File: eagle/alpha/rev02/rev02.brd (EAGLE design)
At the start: 100 x 80 mm, 382 parts, among them CN1 HOST, CN2 HOST, IC1 N25Q128A13ES, IC2 74AC244DW, IC3 N25Q128A13ES, J1 STM32-SWD, Q1 2N7002, Q2 BC818, Q4 2N7002, Q5 ASFL1, Q6 2N7002, T1 BC847, T2 BC847, U1 LMZ13608, U10 ATTINY828R-AU, U11 MC14551BDG, U12 23K640-I/SN, U13 XC7A200TFBG484, U14 EN6347QI, U15 EN6347QI, U16 EN5364QI, U2 LT3060ITS8-15, U3 MC74HC1G14DTT1G, U4 STM32F429BIT6, U5 IS45S32160F, U6 IS45S32160F, U7 MCP79412-I/SN, U8 FT232H_SERIAL, U9 FT232H_SERIAL, Y1 12 MHz, Y2 12 MHz

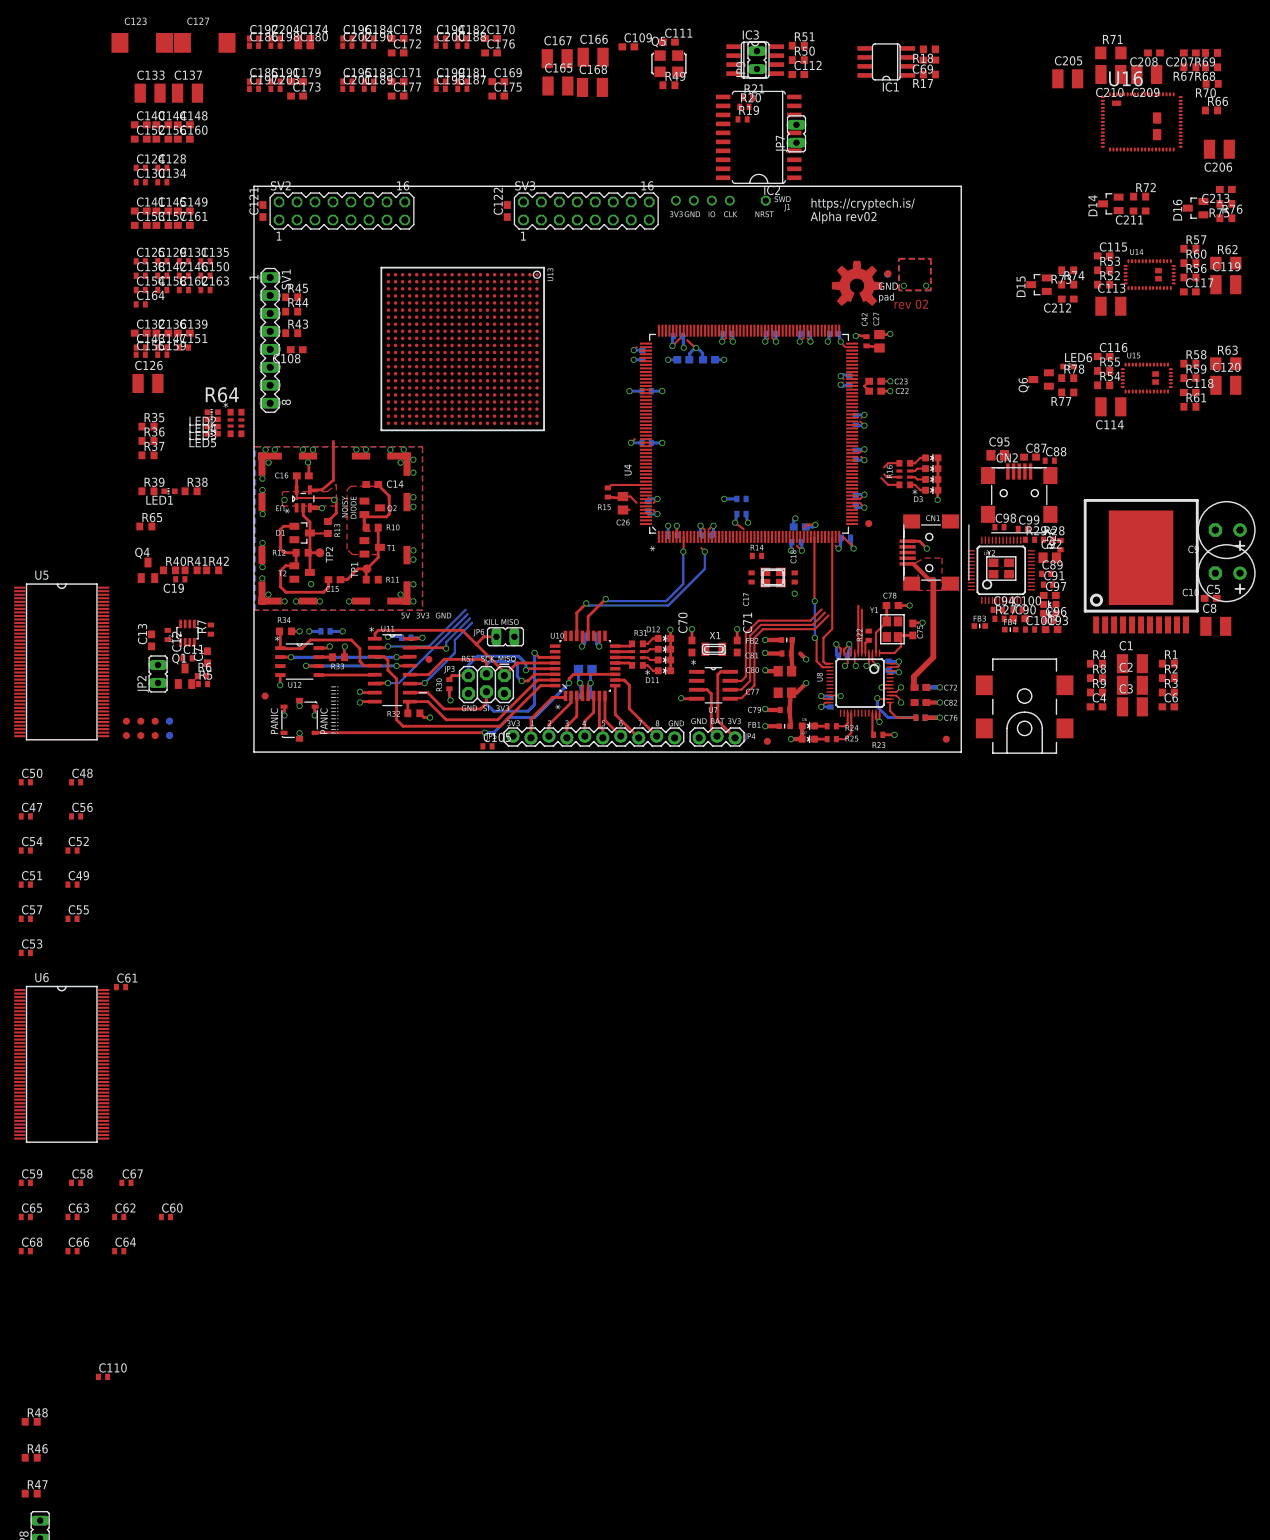
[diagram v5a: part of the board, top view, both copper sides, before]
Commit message: optimize BOM a bit, change more 0603s to 0402s
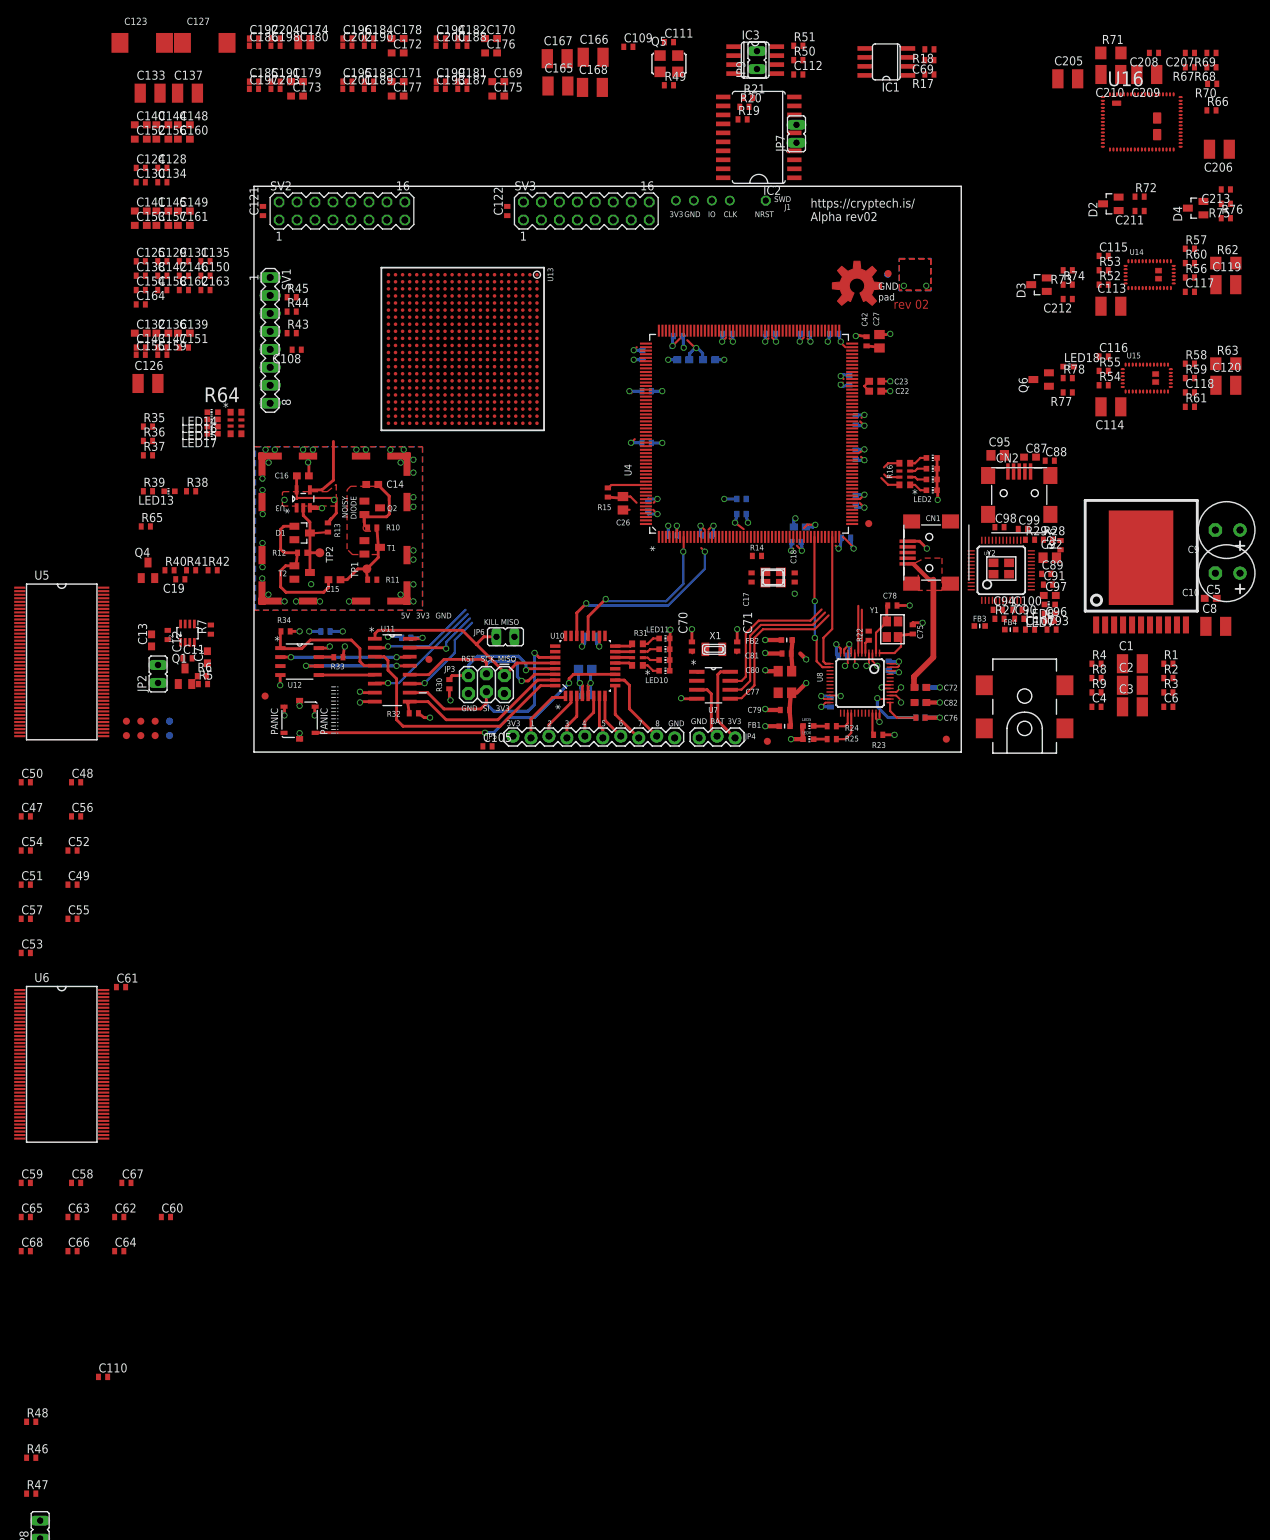
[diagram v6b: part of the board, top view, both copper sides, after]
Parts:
- removed D10, D7, D9: GREEN, SparkFun-LED:LED-0603
- removed D11: RED, SparkFun-LED:LED-0603
- removed D12: BLUE, SparkFun-LED:LED-0603
- removed D13, D5, D6, D8: YELLOW, SparkFun-LED:LED-0603
- removed D14, D15, D16: BAT54, diode:SOT23
- added LED10, LED13, LED14: RED, led:CHIP-LED0603
- added LED11, LED17: BLUE, led:CHIP-LED0603
- added LED12, LED16, LED7: YELLOW, led:CHIP-LED0603
- added LED15, LED18, LED8, LED9: GREEN, led:CHIP-LED0603
- C10, C9: value 330uF -> 330 uF
- C108, C109, C111, C112, C117, C118, C121, C122, C208, C211, C212, C213, C69: device resistor:C0603 -> resistor:C0402
- C11, C12: value 10NF -> 0.01 uF
- C110, C19, C20, C30, C32, C33, C34, C35, C36, C37, C38, C39, C40, C41, C42, C43, C44, C45, C46, C49, C51, C52, C53, C54, C55, C56, C57, C60, C62, C63, C64, C65, C66, C67, C68: value 0.1uF -> 0.1 uF
- C115, C116, C207, C4, C6: value 0.047uF -> 0.047 uF; device resistor:C0603 -> resistor:C0402
- C13, C7: value 2.2 uF LowESR -> 2.2 uF
- C14, C15, C16: device rcl:C0603 -> resistor:C0603
- C5: value 0.47uF -> 0.47 uF
- C70, C71: value 5pF -> 5 pF; device rcl:C0603 -> resistor:C0402
- C75, C78, C90, C93: device rcl:C0603 -> resistor:C0402
- D2: value GREEN -> BAT54; device SparkFun-LED:LED-0603 -> diode:SOT23
- D3: value RED -> BAT54; device SparkFun-LED:LED-0603 -> diode:SOT23
- D4: value BLUE -> BAT54; device SparkFun-LED:LED-0603 -> diode:SOT23
- LED1: value RED -> GREEN
- LED3: value GREEN -> BLUE
- LED5: value BLUE -> YELLOW
- R1, R10, R17, R18, R2, R3, R35, R36, R37, R38, R39, R4, R40, R41, R42, R43, R44, R45, R46, R47, R48, R49, R50, R51, R52, R53, R54, R55, R56, R57, R58, R59, R60, R61, R65, R66, R67, R68, R69, R70, R72, R73, R74, R75, R76, R77, R78, R8, R9: device resistor:R0603 -> resistor:R0402
- R11, R13: value 1K -> 1k; device resistor:R0603 -> resistor:R0402
- R12: value 10K -> 10k; device resistor:R0603 -> resistor:R0402
- R15, R19, R20, R21, R23, R27, R6, R7: value 10K -> 10k
- R22, R26: value 12K -> 12k
- R30: value 15K -> 15k
- R32, R33, R34: value 15K -> 15k; device resistor:R0603 -> resistor:R0402
- R5: value 1K -> 1k
- moved LED1 107.8 mm to (115.9, 40.8), turned to 270 degrees
- moved LED2 102.3 mm to (115.9, 37.7), turned to 270 degrees
- moved LED4 102.0 mm to (115.9, 39.3), turned to 270 degrees
- moved LED3 101.8 mm to (115.9, 42.3), turned to 270 degrees
- moved LED5 93.8 mm to (98.5, 4.41), turned to 270 degrees
- moved LED6 64.2 mm to (98.5, 2.54)
- moved D4 51.4 mm to (153.2, 77.6), turned to 90 degrees
- moved D2 45.2 mm to (141.2, 78.2), turned to 90 degrees
- moved D3 32.8 mm to (131.1, 66.8), turned to 90 degrees
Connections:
- net FPGA_DONE_INT: now also LED13.C; no longer LED1.C
- net FT_MGMT_VCC3V3: now also LED7.A, LED8.A; no longer D8.A, D9.A
- net FT_VCC3V3: now also LED5.A, LED6.A; no longer D6.A, D7.A
- net GND: now also LED1.C, LED10.C, LED11.C, LED12.C, LED14.C, LED15.C, LED16.C, LED17.C, LED9.C; no longer D10.C, D11.C, D12.C, D13.C, D2.C, D3.C, D4.C, D5.C, LED5.C
- net N$15: now also LED12.A; no longer D13.A
- net N$16: now also LED10.A; no longer D11.A
- net N$17: now also LED3.A; no longer D4.A
- net N$18: now also LED1.A; no longer D2.A
- net N$19: now also LED4.A; no longer D5.A
- net N$20: now also LED2.A; no longer D3.A
- net N$24: now also LED5.C; no longer D6.C
- net N$26: now also LED6.C; no longer D7.C
- net N$27: now also LED17.A; no longer LED5.A
- net N$28: now also LED15.A; no longer LED3.A
- net N$29: now also LED16.A; no longer LED4.A
- net N$30: now also LED14.A; no longer LED2.A
- net N$34: now also LED13.A; no longer LED1.A
- net N$4: now also LED11.A; no longer D12.A
- net N$5: now also LED9.A; no longer D10.A
- net N$50: now also LED18.C; no longer LED6.C
- net N$51: now also LED18.A; no longer LED6.A
- net N$6: now also LED7.C; no longer D8.C
- net N$7: now also LED8.C; no longer D9.C
- net POK_VCCAUX: now also D3.3; no longer D15.3
- net POK_VCCINT: now also D4.3; no longer D16.3
- net PWR_ENA_VCCAUX: now also D4.1; no longer D16.1
- net PWR_ENA_VCCINT: now also D2.1; no longer D14.1
- net PWR_ENA_VCCO: now also D3.1; no longer D15.1
- net VCC_5V0: now also D2.3; no longer D14.3
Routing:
- net GND: track 139.6 -> 140.6 mm
- net AMPLIFIED: track 14.0 -> 14.5 mm

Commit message: First set of updates based on review feedback.
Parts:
- removed R17: 4.7k, resistor:R0402
- C13, C7: value 2.2 uF -> 4.7 uF
- R24, R25, R28, R29: value 220 -> 330
- moved R4 198.2 mm to (-11.4, -115.6)
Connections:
- removed net N$53: R4.2, U1.P$3
- new net N$3: Q5.3, R4.2
- net FPGA_GCLK: no longer Q5.3
- net GND: now also C22.1, C23.1, C24.1, C25.1, U1.3, U1.5, U1.6, U1.TP1, U14.13, U14.14, U14.15, U14.16, U14.17, U14.18, U14.32, U15.13, U15.14, U15.15, U15.16, U15.17, U15.18, U15.32, U16.1, U16.2, U16.27, U16.28, U16.29, U16.3, U16.30, U16.31, U16.32, U16.33, U16.4, U16.55, U16.64, U16.65, U16.66, U16.67, U16.68; no longer R17.1, R18.1, R4.1, U1.P$5, U1.P$6, U1.P$8, U14.P$13, U14.P$14, U14.P$15, U14.P$16, U14.P$17, U14.P$18, U14.P$32, U15.P$13, U15.P$14, U15.P$15, U15.P$16, U15.P$17, U15.P$18, U15.P$32, U16.P$1, U16.P$2, U16.P$27, U16.P$28, U16.P$29, U16.P$3, U16.P$30, U16.P$31, U16.P$32, U16.P$33, U16.P$4, U16.P$55, U16.P$64, U16.P$65, U16.P$66, U16.P$67, U16.P$68
- net KSM_PROM_CS_N: now also U4.61
- net N$35: now also U14.30; no longer U14.P$30
- net N$36: now also U14.29; no longer U14.P$29
- net N$37: now also U14.26; no longer U14.P$26
- net N$38: now also U14.10, U14.11, U14.5, U14.6, U14.7, U14.8, U14.9; no longer U14.P$10, U14.P$11, U14.P$5, U14.P$6, U14.P$7, U14.P$8, U14.P$9
- net N$39: now also U14.31; no longer U14.P$31
- net N$40: now also U15.30; no longer U15.P$30
- net N$41: now also U15.29; no longer U15.P$29
- net N$42: now also U15.26; no longer U15.P$26
- net N$43: now also U15.10, U15.11, U15.5, U15.6, U15.7, U15.8, U15.9; no longer U15.P$10, U15.P$11, U15.P$5, U15.P$6, U15.P$7, U15.P$8, U15.P$9
- net N$44: now also U15.31; no longer U15.P$31
- net N$45: now also U16.59; no longer U16.P$59
- net N$46: now also U16.51; no longer U16.P$51
- net N$47: now also U16.63; no longer U16.P$63
- net N$48: now also U16.10, U16.11, U16.12, U16.13, U16.5, U16.6, U16.7, U16.8, U16.9; no longer U16.P$10, U16.P$11, U16.P$12, U16.P$13, U16.P$5, U16.P$6, U16.P$7, U16.P$8, U16.P$9
- net N$49: now also U16.56; no longer U16.P$56
- net N$52: now also U1.8; no longer U1.P$9
- net N$55: now also U1.4; no longer U1.P$4
- net N$56: now also U1.7; no longer U1.P$7
- net POK_VCCAUX: now also U14.28; no longer U14.P$28
- net POK_VCCINT: now also U16.54; no longer U16.P$54
- net POK_VCCO: now also U15.28; no longer U15.P$28
- net PWR_18V: now also U1.1, U1.2; no longer U1.P$1, U1.P$2
- net PWR_ENA_VCCAUX: now also U14.27; no longer U14.P$27
- net PWR_ENA_VCCINT: now also U16.52; no longer U16.P$52
- net PWR_ENA_VCCO: now also U15.27; no longer U15.P$27
- net VCCO_3V3: now also R18.1; no longer C22.1, C23.1, C24.1, C25.1, R17.2
- net VCC_5V0: now also U1.10, U1.11, U14.19, U14.20, U14.21, U14.33, U15.19, U15.20, U15.21, U15.33, U16.34, U16.35, U16.36, U16.37, U16.38, U16.39, U16.40, U16.41, U16.42, U16.43, U16.53; no longer U1.P$11, U1.P$12, U14.P$19, U14.P$20, U14.P$21, U14.P$33, U15.P$19, U15.P$20, U15.P$21, U15.P$33, U16.P$34, U16.P$35, U16.P$36, U16.P$37, U16.P$38, U16.P$39, U16.P$40, U16.P$41, U16.P$42, U16.P$43, U16.P$53
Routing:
- net VCCO_3V3: track 79.4 -> 74.3 mm, vias 25 -> 21
